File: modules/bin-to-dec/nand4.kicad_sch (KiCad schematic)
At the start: 4 parts, among them Q10 2N7002, Q11 2N7002, Q12 DMP3099L, Q9 DMP3099L

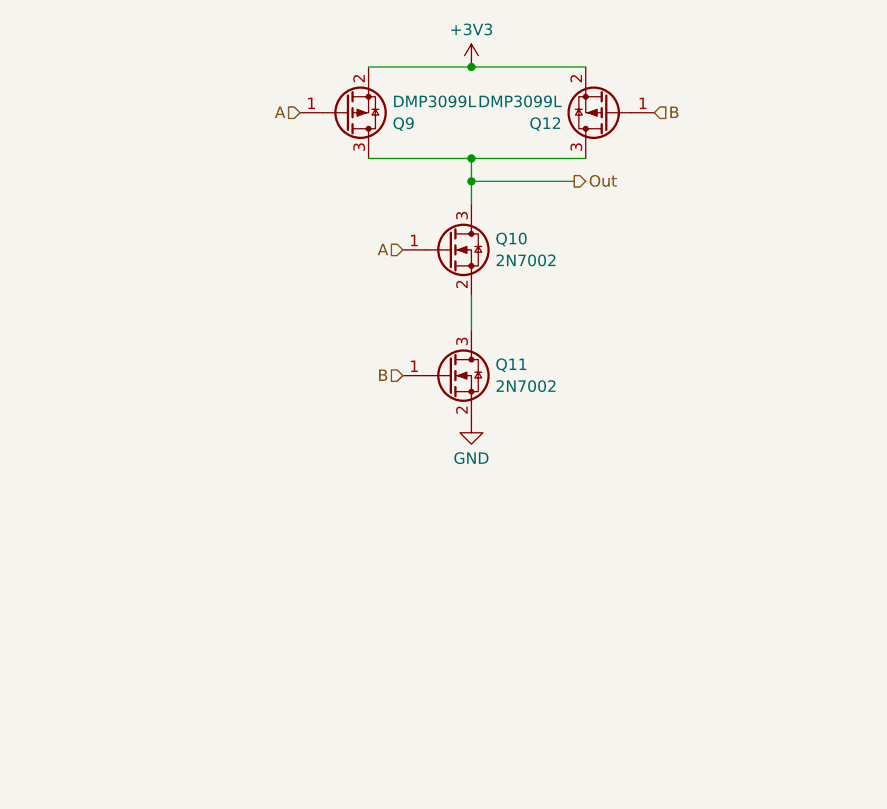
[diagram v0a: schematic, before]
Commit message: move to correct dir. improved symmetry of pcb
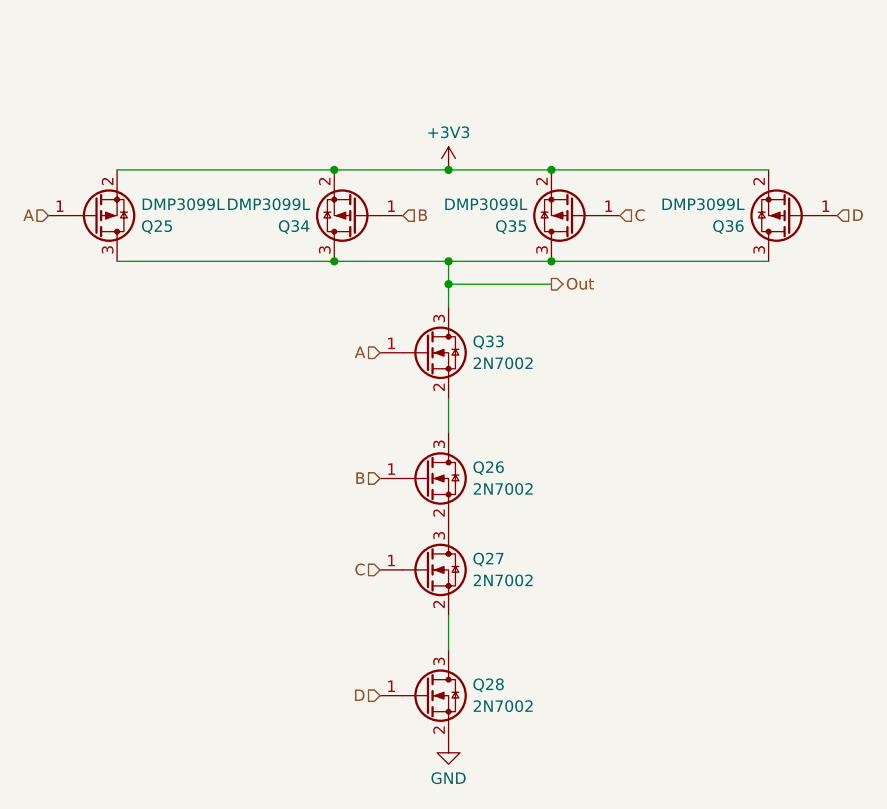
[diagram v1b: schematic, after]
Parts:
- removed Q10, Q11: 2N7002, Package_TO_SOT_SMD:SOT-23, symbol Transistor_FET:2N7002
- removed Q12, Q9: DMP3099L, Package_TO_SOT_SMD:SOT-23, symbol Transistor_FET:DMP3099L
- added Q25, Q34, Q35, Q36: DMP3099L, Package_TO_SOT_SMD:SOT-23, symbol Transistor_FET:DMP3099L
- added Q26, Q27, Q28, Q33: 2N7002, Package_TO_SOT_SMD:SOT-23, symbol Transistor_FET:2N7002
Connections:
- net +3V3: now also Q25.2 (S), Q34.2 (S), Q35.2 (S), Q36.2 (S)
- net A: now also Q25.1 (G), Q33.1 (G)
- net B: now also Q26.1 (G), Q34.1 (G)
- net GND: now also Q28.2 (S)
- net Out: now also Q25.3 (D), Q33.3 (D), Q34.3 (D), Q35.3 (D), Q36.3 (D)
- new net: Q27.2 (S), Q28.3 (D)
- new net: Q26.3 (D), Q33.2 (S)
- new net: Q26.2 (S), Q27.3 (D)
- new net C: Q27.1 (G), Q35.1 (G)
- new net D: Q28.1 (G), Q36.1 (G)

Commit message: using plugin to generate jlc production files
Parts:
- Q25, Q34, Q35, Q36: LCSC Part # (none) -> C2940610
- Q26, Q27, Q28, Q33: LCSC Part # (none) -> C8545
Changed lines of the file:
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@@
+			)
+		)
+		(property "LCSC Part #" "C8545"
+			(at 142.24 125.73 0)
+			(effects
+				(font
+					(size 1.27 1.27)
+				)
+				(hide yes)
 			)
 		)
@@
 			)
 		)
+		(property "LCSC Part #" "C8545"
+			(at 142.24 87.63 0)
+			(effects
+				(font
+					(size 1.27 1.27)
+				)
+				(hide yes)
+			)
+		)
 		(pin "1"
 		)
@@
 			)
 		)
+		(property "LCSC Part #" "C2940610"
+			(at 134.62 72.39 0)
+			(effects
+				(font
+					(size 1.27 1.27)
+				)
+				(hide yes)
+			)
+		)
 		(pin "2"
 		)
@@
 		)
 		(property "Description" "-3.8A Id, -30V Vds, P-Channel MOSFET, SOT-23"
+			(at 182.88 72.39 0)
+			(effects
+				(font
+					(size 1.27 1.27)
+				)
+				(hide yes)
+			)
+		)
+		(property "LCSC Part #" "C2940610"
 			(at 182.88 72.39 0)
 			(effects
@@
 			)
 		)
+		(property "LCSC Part #" "C2940610"
+			(at 105.41 72.39 0)
+			(effects
+				(font
+					(size 1.27 1.27)
+				)
+				(hide yes)
+			)
+		)
 		(pin "2"
 		)
@@
 		)
 		(property "Description" "-3.8A Id, -30V Vds, P-Channel MOSFET, SOT-23"
+			(at 158.75 72.39 0)
+			(effects
+				(font
+					(size 1.27 1.27)
+				)
+				(hide yes)
+			)
+		)
+		(property "LCSC Part #" "C2940610"
 			(at 158.75 72.39 0)
 			(effects
@@
 			)
 		)
+		(property "LCSC Part #" "C8545"
+			(at 142.24 101.6 0)
+			(effects
+				(font
+					(size 1.27 1.27)
+				)
+				(hide yes)
+			)
+		)
 		(pin "1"
 		)
@@
 			(at 142.24 111.76 0)
 			(effects
+				(font
+					(size 1.27 1.27)
+				)
+				(hide yes)
+			)
+		)
+		(property "LCSC Part #" "C8545"
+			(at 142.24 111.76 0)
+			(effects

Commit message: move components to top layer :(
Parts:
- Q12: renamed from Q25; LCSC part number (none) -> C2940610
- Q16: renamed from Q26; LCSC part number (none) -> C8545
- Q54: renamed from Q36; LCSC part number (none) -> C2940610
- Q55: renamed from Q35; LCSC part number (none) -> C2940610
- Q58: renamed from Q33; LCSC part number (none) -> C8545
- Q59: renamed from Q34; LCSC part number (none) -> C2940610
- Q6: renamed from Q28; LCSC part number (none) -> C8545
- Q7: renamed from Q27; LCSC part number (none) -> C8545
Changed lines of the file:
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@@
 		(dnp no)
 		(fields_autoplaced yes)
-		(property "Reference" "Q28"
+		(property "Reference" "Q6"
 			(at 147.447 124.5178 0)
 			(effects
@@
 			)
 		)
+		(property "LCSC part number" "C8545"
+			(at 142.24 125.73 0)
+			(effects
+				(font
+					(size 1.27 1.27)
+				)
+				(hide yes)
+			)
+		)
 		(pin "1"
 		)
@@
 			(project "bin-to-dec"
 				(path "/b244e12b-f85f-4579-ba5e-848643f54694/0df26d3b-1463-4745-9b60-c38ec60dc515"
-					(reference "Q28")
+					(reference "Q6")
 					(unit 1)
 				)
@@
 		(dnp no)
 		(fields_autoplaced yes)
-		(property "Reference" "Q33"
+		(property "Reference" "Q58"
 			(at 147.447 86.4178 0)
 			(effects
@@
 			)
 		)
+		(property "LCSC part number" "C8545"
+			(at 142.24 87.63 0)
+			(effects
+				(font
+					(size 1.27 1.27)
+				)
+				(hide yes)
+			)
+		)
 		(pin "1"
 		)
@@
 			(project "bin-to-dec"
 				(path "/b244e12b-f85f-4579-ba5e-848643f54694/0df26d3b-1463-4745-9b60-c38ec60dc515"
-					(reference "Q33")
+					(reference "Q58")
 					(unit 1)
 				)
@@
 		(on_board yes)
 		(dnp no)
-		(property "Reference" "Q34"
+		(property "Reference" "Q59"
 			(at 129.413 73.6022 0)
 			(effects
@@
 			)
 		)
+		(property "LCSC part number" "C2940610"
+			(at 134.62 72.39 0)
+			(effects
+				(font
+					(size 1.27 1.27)
+				)
+				(hide yes)
+			)
+		)
 		(pin "2"
 		)
@@
 			(project "bin-to-dec"
 				(path "/b244e12b-f85f-4579-ba5e-848643f54694/0df26d3b-1463-4745-9b60-c38ec60dc515"
-					(reference "Q34")
+					(reference "Q59")
 					(unit 1)
 				)
@@
 		(on_board yes)
 		(dnp no)
-		(property "Reference" "Q36"
+		(property "Reference" "Q54"
 			(at 177.673 73.6022 0)
 			(effects
@@
 			)
 		)
+		(property "LCSC part number" "C2940610"
+			(at 182.88 72.39 0)
+			(effects
+				(font
+					(size 1.27 1.27)
+				)
+				(hide yes)
+			)
+		)
 		(pin "2"
 		)
@@
 			(project "bin-to-dec"
 				(path "/b244e12b-f85f-4579-ba5e-848643f54694/0df26d3b-1463-4745-9b60-c38ec60dc515"
-					(reference "Q36")
+					(reference "Q54")
 					(unit 1)
 				)
@@
 		(on_board yes)
 		(dnp no)
-		(property "Reference" "Q25"
+		(property "Reference" "Q12"
 			(at 110.617 73.6022 0)
 			(effects
@@
 			)
 		)
+		(property "LCSC part number" "C2940610"
+			(at 105.41 72.39 0)
+			(effects
+				(font
+					(size 1.27 1.27)
+				)
+				(hide yes)
+			)
+		)
 		(pin "2"
 		)
@@
 			(project "bin-to-dec"
 				(path "/b244e12b-f85f-4579-ba5e-848643f54694/0df26d3b-1463-4745-9b60-c38ec60dc515"
-					(reference "Q25")
+					(reference "Q12")
 					(unit 1)
 				)
@@
 		(on_board yes)
 		(dnp no)
-		(property "Reference" "Q35"
+		(property "Reference" "Q55"
 			(at 153.543 73.6022 0)
 			(effects
@@
 			)
 		)
+		(property "LCSC part number" "C2940610"
+			(at 158.75 72.39 0)
+			(effects
+				(font
+					(size 1.27 1.27)
+				)
+				(hide yes)
+			)
+		)
 		(pin "2"
 		)
@@
 			(project "bin-to-dec"
 				(path "/b244e12b-f85f-4579-ba5e-848643f54694/0df26d3b-1463-4745-9b60-c38ec60dc515"
-					(reference "Q35")
+					(reference "Q55")
 					(unit 1)
 				)
@@
 		(dnp no)
 		(fields_autoplaced yes)
-		(property "Reference" "Q26"
+		(property "Reference" "Q16"
 			(at 147.447 100.3878 0)
 			(effects
@@
 			)
 		)
+		(property "LCSC part number" "C8545"
+			(at 142.24 101.6 0)
+			(effects
+				(font
+					(size 1.27 1.27)
+				)
+				(hide yes)
+			)
+		)
 		(pin "1"
 		)
@@
 			(project "bin-to-dec"
 				(path "/b244e12b-f85f-4579-ba5e-848643f54694/0df26d3b-1463-4745-9b60-c38ec60dc515"
-					(reference "Q26")
+					(reference "Q16")
 					(unit 1)
 				)
@@
 		(dnp no)
 		(fields_autoplaced yes)
-		(property "Reference" "Q27"
+		(property "Reference" "Q7"
 			(at 147.447 110.5478 0)
 			(effects
@@
 			)
 		)
+		(property "LCSC part number" "C8545"
+			(at 142.24 111.76 0)
+			(effects
+				(font
+					(size 1.27 1.27)
+				)
+				(hide yes)
+			)
+		)
 		(pin "1"
 		)
@@
 			(project "bin-to-dec"
 				(path "/b244e12b-f85f-4579-ba5e-848643f54694/0df26d3b-1463-4745-9b60-c38ec60dc515"
-					(reference "Q27")
-					(unit 1)
-				)
+					(reference "Q7")
+					(unit 1)
+				)

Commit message: switched to jlc basic components
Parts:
- Q12, Q54, Q55, Q59: value DMP3099L -> AO3401A; LCSC Part # C2940610 -> C15127
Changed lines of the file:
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@@
 			)
 		)
-		(property "Value" "DMP3099L"
+		(property "Value" "AO3401A"
 			(at 129.413 71.1779 0)
 			(effects
@@
 			)
 		)
-		(property "Datasheet" "https://www.diodes.com/assets/Datasheets/DMP3099L.pdf"
+		(property "Datasheet" "https://jlcpcb.com/api/file/downloadByFileSystemAccessId/8553305450243108864"
 			(at 129.54 68.58 0)
 			(effects
@@
 			)
 		)
-		(property "LCSC Part #" "C2940610"
+		(property "LCSC Part #" "C15127"
 			(at 134.62 72.39 0)
 			(effects
@@
 			)
 		)
-		(property "Value" "DMP3099L"
+		(property "Value" "AO3401A"
 			(at 177.673 71.1779 0)
 			(effects
@@
 			)
 		)
-		(property "Datasheet" "https://www.diodes.com/assets/Datasheets/DMP3099L.pdf"
+		(property "Datasheet" "https://jlcpcb.com/api/file/downloadByFileSystemAccessId/8553305450243108864"
 			(at 177.8 68.58 0)
 			(effects
@@
 			)
 		)
-		(property "LCSC Part #" "C2940610"
+		(property "LCSC Part #" "C15127"
 			(at 182.88 72.39 0)
 			(effects
@@
 			)
 		)
-		(property "Value" "DMP3099L"
+		(property "Value" "AO3401A"
 			(at 110.617 71.1779 0)
 			(effects
@@
 			)
 		)
-		(property "Datasheet" "https://www.diodes.com/assets/Datasheets/DMP3099L.pdf"
+		(property "Datasheet" "https://jlcpcb.com/api/file/downloadByFileSystemAccessId/8553305450243108864"
 			(at 110.49 68.58 0)
 			(effects
@@
 			)
 		)
-		(property "LCSC Part #" "C2940610"
+		(property "LCSC Part #" "C15127"
 			(at 105.41 72.39 0)
 			(effects
@@
 			)
 		)
-		(property "Value" "DMP3099L"
+		(property "Value" "AO3401A"
 			(at 153.543 71.1779 0)
 			(effects
@@
 			)
 		)
-		(property "Datasheet" "https://www.diodes.com/assets/Datasheets/DMP3099L.pdf"
+		(property "Datasheet" "https://jlcpcb.com/api/file/downloadByFileSystemAccessId/8553305450243108864"
 			(at 153.67 68.58 0)
 			(effects
@@
 			)
 		)
-		(property "LCSC Part #" "C2940610"
+		(property "LCSC Part #" "C15127"
 			(at 158.75 72.39 0)
 			(effects

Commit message: minor edits
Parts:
- Q12, Q54, Q55, Q59: LCSC part number C2940610 -> (none)
- Q16, Q58, Q6, Q7: LCSC part number C8545 -> (none)
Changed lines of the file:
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@@
-			)
-		)
-		(property "LCSC part number" "C8545"
-			(at 142.24 125.73 0)
-			(effects
-				(font
-					(size 1.27 1.27)
-				)
-				(hide yes)
 			)
 		)
@@
 			)
 		)
-		(property "LCSC part number" "C8545"
-			(at 142.24 87.63 0)
-			(effects
-				(font
-					(size 1.27 1.27)
-				)
-				(hide yes)
-			)
-		)
 		(pin "1"
 		)
@@
 			)
 		)
-		(property "LCSC part number" "C2940610"
-			(at 134.62 72.39 0)
-			(effects
-				(font
-					(size 1.27 1.27)
-				)
-				(hide yes)
-			)
-		)
 		(pin "2"
 		)
@@
 		)
 		(property "LCSC Part #" "C15127"
-			(at 182.88 72.39 0)
-			(effects
-				(font
-					(size 1.27 1.27)
-				)
-				(hide yes)
-			)
-		)
-		(property "LCSC part number" "C2940610"
 			(at 182.88 72.39 0)
 			(effects
@@
 			)
 		)
-		(property "LCSC part number" "C2940610"
-			(at 105.41 72.39 0)
-			(effects
-				(font
-					(size 1.27 1.27)
-				)
-				(hide yes)
-			)
-		)
 		(pin "2"
 		)
@@
 		)
 		(property "LCSC Part #" "C15127"
-			(at 158.75 72.39 0)
-			(effects
-				(font
-					(size 1.27 1.27)
-				)
-				(hide yes)
-			)
-		)
-		(property "LCSC part number" "C2940610"
 			(at 158.75 72.39 0)
 			(effects
@@
 			)
 		)
-		(property "LCSC part number" "C8545"
-			(at 142.24 101.6 0)
-			(effects
-				(font
-					(size 1.27 1.27)
-				)
-				(hide yes)
-			)
-		)
 		(pin "1"
 		)
@@
 			(at 142.24 111.76 0)
 			(effects
-				(font
-					(size 1.27 1.27)
-				)
-				(hide yes)
-			)
-		)
-		(property "LCSC part number" "C8545"
-			(at 142.24 111.76 0)
-			(effects
